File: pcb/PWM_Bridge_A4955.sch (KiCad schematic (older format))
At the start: 14 parts, among them Q3 IPD220N06L3, Q4 IPD220N06L3, Q5 IPD220N06L3, Q6 IPD220N06L3, U5 A4955GLPTR-T

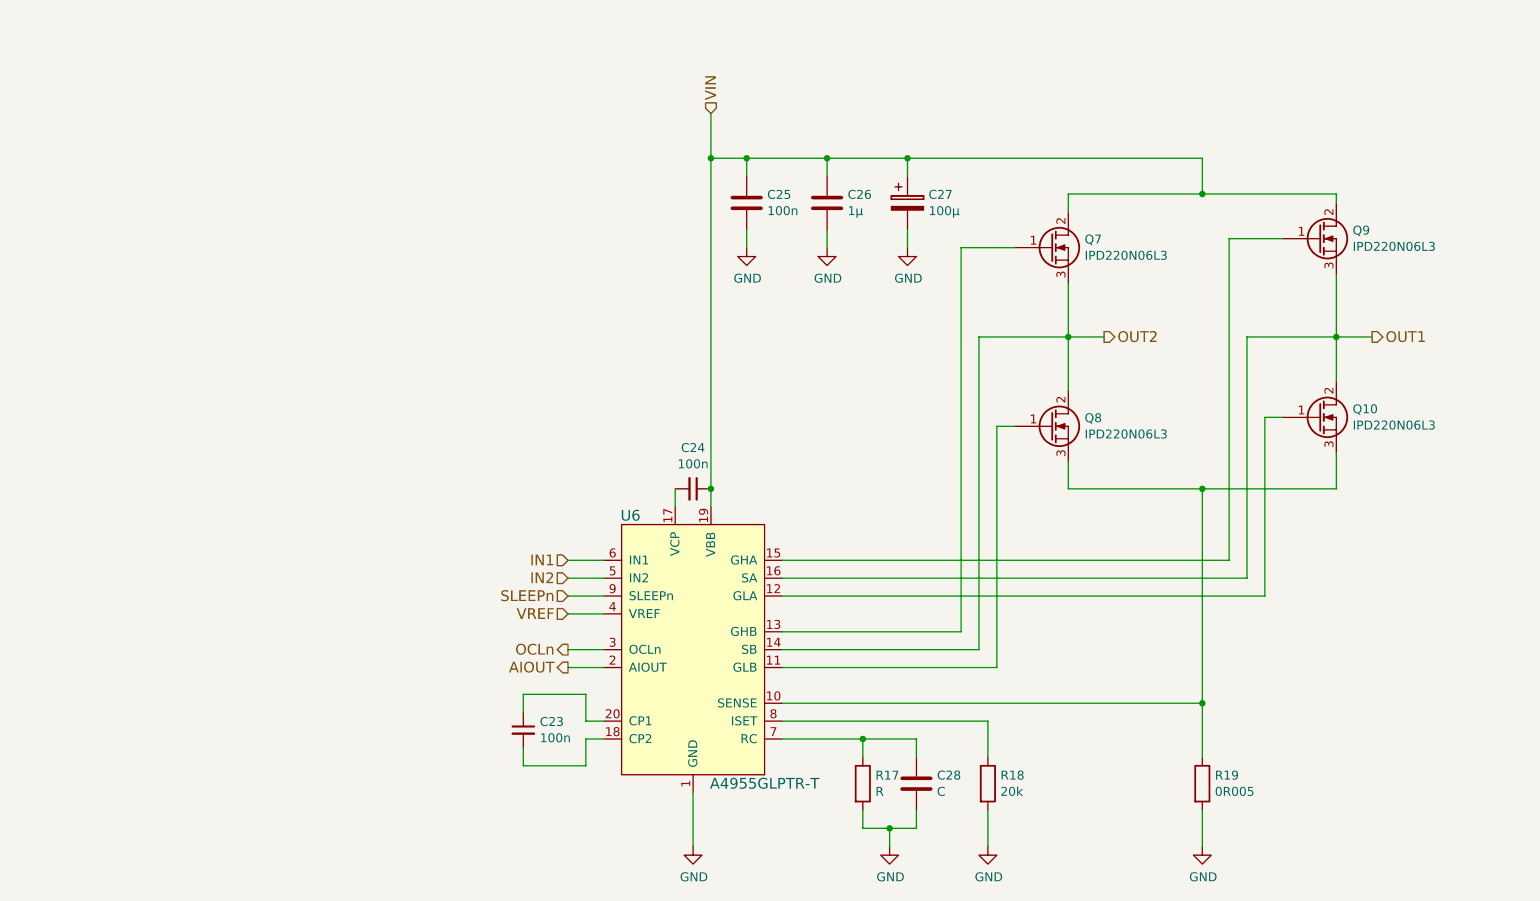
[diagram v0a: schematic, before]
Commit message: Place some components onto the PCB
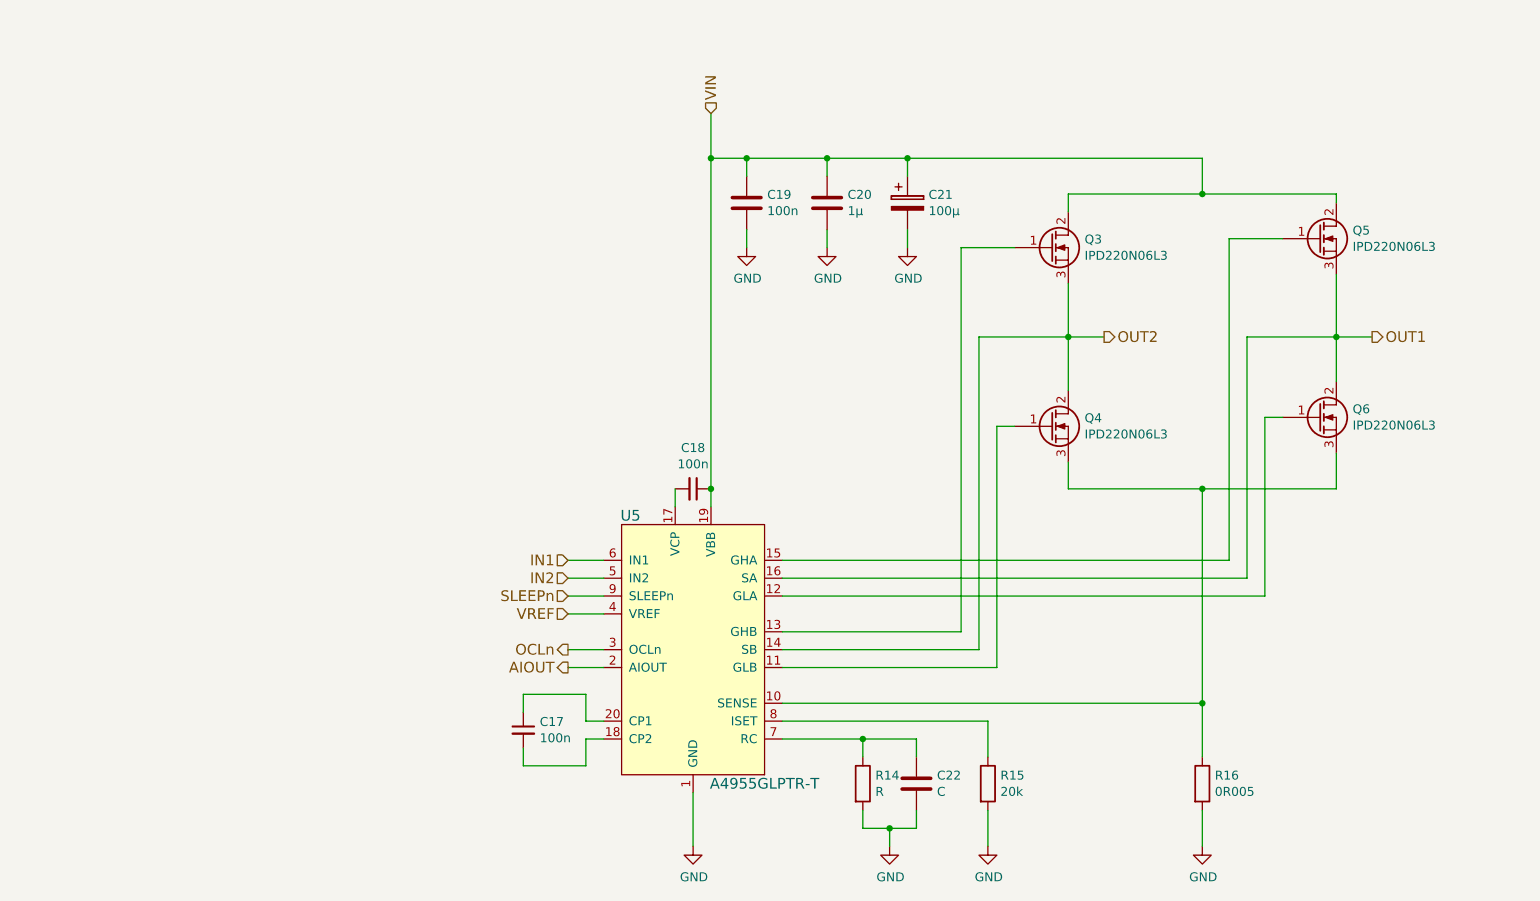
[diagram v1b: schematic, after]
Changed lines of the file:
@@
 AR Path="/58077727/58077F1C" Ref="U5"  Part="1"
 AR Path="/58084D17/58077F1C" Ref="U6"  Part="1"
-F 0 "U6" H 4300 5150 60  0000 C CNN
+F 0 "U5" H 4300 5150 60  0000 C CNN
 F 1 "A4955GLPTR-T" H 5050 3650 60  0000 C CNN
 F 2 "Housings_SSOP:TSSOP-20_4.4x6.5mm_Pitch0.65mm" H 4650 4400 60  0001 C CNN
@@
 AR Path="/58077727/5807829A" Ref="C18"  Part="1"
 AR Path="/58084D17/5807829A" Ref="C24"  Part="1"
-F 0 "C24" V 4421 3500 50  0000 C CNN
+F 0 "C18" V 4421 3500 50  0000 C CNN
 F 1 "100n" V 4512 3500 50  0000 C CNN
 F 2 "Capacitors_SMD:C_0603" H 4650 3500 50  0001 C CNN
@@
 AR Path="/58077727/58078520" Ref="R14"  Part="1"
 AR Path="/58084D17/58078520" Ref="R17"  Part="1"
-F 0 "R17" H 5670 5196 50  0000 L CNN
+F 0 "R14" H 5670 5196 50  0000 L CNN
 F 1 "R" H 5670 5105 50  0000 L CNN
 F 2 "Resistors_SMD:R_0603" V 5530 5150 50  0001 C CNN
@@
 AR Path="/58077727/5807867B" Ref="C22"  Part="1"
 AR Path="/58084D17/5807867B" Ref="C28"  Part="1"
-F 0 "C28" H 6015 5196 50  0000 L CNN
+F 0 "C22" H 6015 5196 50  0000 L CNN
 F 1 "C" H 6015 5105 50  0000 L CNN
 F 2 "Capacitors_SMD:C_0603" H 5938 5000 50  0001 C CNN
@@
 AR Path="/58077727/580787DB" Ref="#PWR053"  Part="1"
 AR Path="/58084D17/580787DB" Ref="#PWR060"  Part="1"
-F 0 "#PWR060" H 5750 5250 50  0001 C CNN
+F 0 "#PWR053" H 5750 5250 50  0001 C CNN
 F 1 "GND" H 5755 5327 50  0000 C CNN
 F 2 "" H 5750 5500 50  0000 C CNN
@@
 AR Path="/58077727/58078835" Ref="#PWR054"  Part="1"
 AR Path="/58084D17/58078835" Ref="#PWR061"  Part="1"
-F 0 "#PWR061" H 4650 5250 50  0001 C CNN
+F 0 "#PWR054" H 4650 5250 50  0001 C CNN
 F 1 "GND" H 4655 5327 50  0000 C CNN
 F 2 "" H 4650 5500 50  0000 C CNN
@@
 AR Path="/58077727/580789CE" Ref="R16"  Part="1"
 AR Path="/58084D17/580789CE" Ref="R19"  Part="1"
-F 0 "R19" H 7570 5196 50  0000 L CNN
+F 0 "R16" H 7570 5196 50  0000 L CNN
 F 1 "0R005" H 7570 5105 50  0000 L CNN
 F 2 "Resistors_SMD:R_2512" V 7430 5150 50  0001 C CNN
@@
 AR Path="/58077727/58078AB1" Ref="#PWR055"  Part="1"
 AR Path="/58084D17/58078AB1" Ref="#PWR062"  Part="1"
-F 0 "#PWR062" H 7500 5250 50  0001 C CNN
+F 0 "#PWR055" H 7500 5250 50  0001 C CNN
 F 1 "GND" H 7505 5327 50  0000 C CNN
 F 2 "" H 7500 5500 50  0000 C CNN
@@
 AR Path="/58077727/58078C46" Ref="Q3"  Part="1"
 AR Path="/58084D17/58078C46" Ref="Q7"  Part="1"
-F 0 "Q7" H 6841 2196 50  0000 L CNN
+F 0 "Q3" H 6841 2196 50  0000 L CNN
 F 1 "IPD220N06L3" H 6841 2105 50  0000 L CNN
 F 2 "TO_SOT_Packages_SMD:TO-252-2Lead" H 6850 2250 50  0001 C CNN
@@
 AR Path="/58077727/58078E80" Ref="Q5"  Part="1"
 AR Path="/58084D17/58078E80" Ref="Q9"  Part="1"
-F 0 "Q9" H 8341 2146 50  0000 L CNN
+F 0 "Q5" H 8341 2146 50  0000 L CNN
 F 1 "IPD220N06L3" H 8341 2055 50  0000 L CNN
 F 2 "TO_SOT_Packages_SMD:TO-252-2Lead" H 8350 2200 50  0001 C CNN
@@
 AR Path="/58077727/58078ED9" Ref="Q6"  Part="1"
 AR Path="/58084D17/58078ED9" Ref="Q10"  Part="1"
-F 0 "Q10" H 8341 3146 50  0000 L CNN
+F 0 "Q6" H 8341 3146 50  0000 L CNN
 F 1 "IPD220N06L3" H 8341 3055 50  0000 L CNN
 F 2 "TO_SOT_Packages_SMD:TO-252-2Lead" H 8350 3200 50  0001 C CNN
@@
 AR Path="/58077727/58078F3F" Ref="Q4"  Part="1"
 AR Path="/58084D17/58078F3F" Ref="Q8"  Part="1"
-F 0 "Q8" H 6841 3196 50  0000 L CNN
+F 0 "Q4" H 6841 3196 50  0000 L CNN
 F 1 "IPD220N06L3" H 6841 3105 50  0000 L CNN
 F 2 "TO_SOT_Packages_SMD:TO-252-2Lead" H 6850 3250 50  0001 C CNN
@@
 AR Path="/58077727/5807A394" Ref="C19"  Part="1"
 AR Path="/58084D17/5807A394" Ref="C25"  Part="1"
-F 0 "C25" H 5065 1946 50  0000 L CNN
+F 0 "C19" H 5065 1946 50  0000 L CNN
 F 1 "100n" H 5065 1855 50  0000 L CNN
 F 2 "Capacitors_SMD:C_0603" H 4988 1750 50  0001 C CNN
@@
 AR Path="/58077727/5807A4C6" Ref="#PWR056"  Part="1"
 AR Path="/58084D17/5807A4C6" Ref="#PWR063"  Part="1"
-F 0 "#PWR063" H 4950 1900 50  0001 C CNN
+F 0 "#PWR056" H 4950 1900 50  0001 C CNN
 F 1 "GND" H 4955 1977 50  0000 C CNN
 F 2 "" H 4950 2150 50  0000 C CNN
@@
 AR Path="/58077727/5807A62E" Ref="C21"  Part="1"
 AR Path="/58084D17/5807A62E" Ref="C27"  Part="1"
-F 0 "C27" H 5968 1946 50  0000 L CNN
+F 0 "C21" H 5968 1946 50  0000 L CNN
 F 1 "100µ" H 5968 1855 50  0000 L CNN
 F 2 "Capacitors_SMD:c_elec_10x10" H 5888 1750 50  0001 C CNN
@@
 AR Path="/58077727/5807A964" Ref="#PWR057"  Part="1"
 AR Path="/58084D17/5807A964" Ref="#PWR064"  Part="1"
-F 0 "#PWR064" H 5850 1900 50  0001 C CNN
+F 0 "#PWR057" H 5850 1900 50  0001 C CNN
 F 1 "GND" H 5855 1977 50  0000 C CNN
 F 2 "" H 5850 2150 50  0000 C CNN
@@
 AR Path="/58077727/5807BEA4" Ref="C17"  Part="1"
 AR Path="/58084D17/5807BEA4" Ref="C23"  Part="1"
-F 0 "C23" H 3792 4896 50  0000 L CNN
+F 0 "C17" H 3792 4896 50  0000 L CNN
 F 1 "100n" H 3792 4805 50  0000 L CNN
 F 2 "Capacitors_SMD:C_0603" H 3700 4850 50  0001 C CNN
@@
 AR Path="/58077727/5809AC71" Ref="C20"  Part="1"
 AR Path="/58084D17/5809AC71" Ref="C26"  Part="1"
-F 0 "C26" H 5515 1946 50  0000 L CNN
+F 0 "C20" H 5515 1946 50  0000 L CNN
 F 1 "1µ" H 5515 1855 50  0000 L CNN
 F 2 "Capacitors_SMD:C_0603" H 5438 1750 50  0001 C CNN
@@
 AR Path="/58084D17/5809ACB6" Ref="#PWR065"  Part="1"
 AR Path="/58077727/5809ACB6" Ref="#PWR058"  Part="1"
-F 0 "#PWR065" H 5400 1900 50  0001 C CNN
+F 0 "#PWR058" H 5400 1900 50  0001 C CNN
 F 1 "GND" H 5405 1977 50  0000 C CNN
 F 2 "" H 5400 2150 50  0000 C CNN
@@
 AR Path="/58077727/580A461C" Ref="R15"  Part="1"
 AR Path="/58084D17/580A461C" Ref="R18"  Part="1"
-F 0 "R18" H 6370 5196 50  0000 L CNN
+F 0 "R15" H 6370 5196 50  0000 L CNN
 F 1 "20k" H 6370 5105 50  0000 L CNN
 F 2 "Resistors_SMD:R_0603" V 6230 5150 50  0001 C CNN
@@
 AR Path="/58077727/580A46B3" Ref="#PWR059"  Part="1"
 AR Path="/58084D17/580A46B3" Ref="#PWR066"  Part="1"
-F 0 "#PWR066" H 6300 5250 50  0001 C CNN
+F 0 "#PWR059" H 6300 5250 50  0001 C CNN
 F 1 "GND" H 6305 5327 50  0000 C CNN
 F 2 "" H 6300 5500 50  0000 C CNN

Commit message: Improve pcb routing, add testpoints and etc. The design improves a lot. Still lots to do, but most important design parts should now be drafted almost complete.
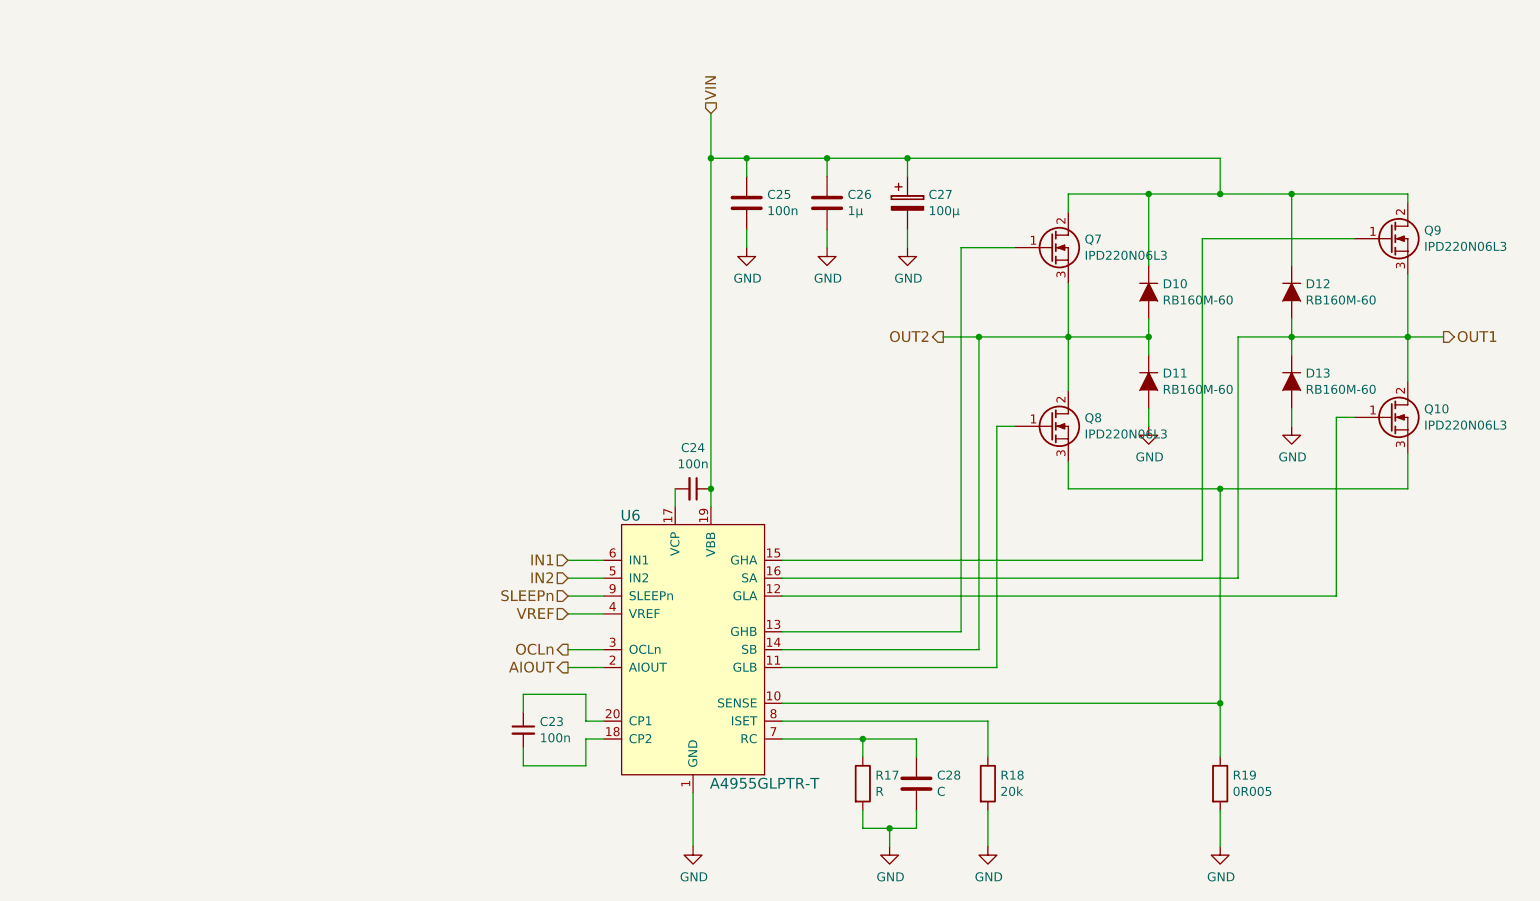
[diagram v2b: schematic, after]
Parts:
- added D6, D7, D8, D9: RB160M-60, Diodes_SMD:SOD-123, symbol D
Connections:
- net GND: now also D7.2 (A), D9.2 (A)
- net OUT1: now also D8.2 (A), D9.1 (K)
- net OUT2: now also D6.2 (A), D7.1 (K)
- net VIN: now also D6.1 (K), D8.1 (K)
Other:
- moved on the sheet: Q10, Q9, R19
